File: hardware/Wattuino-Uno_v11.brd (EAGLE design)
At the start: 68.6 x 53.3 mm, 61 parts, among them IC1 ATMEGA328-PU, IC2 FT231XQ, IC3 LDO-TS1117CW-5V, IC4 LDO-TS9011-3V3, J2 USB-B-H, J3 USB-MICRO, Q1 16MHz, X1 PASSER-07, X2 PASSER-07, X3 PASSER-07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

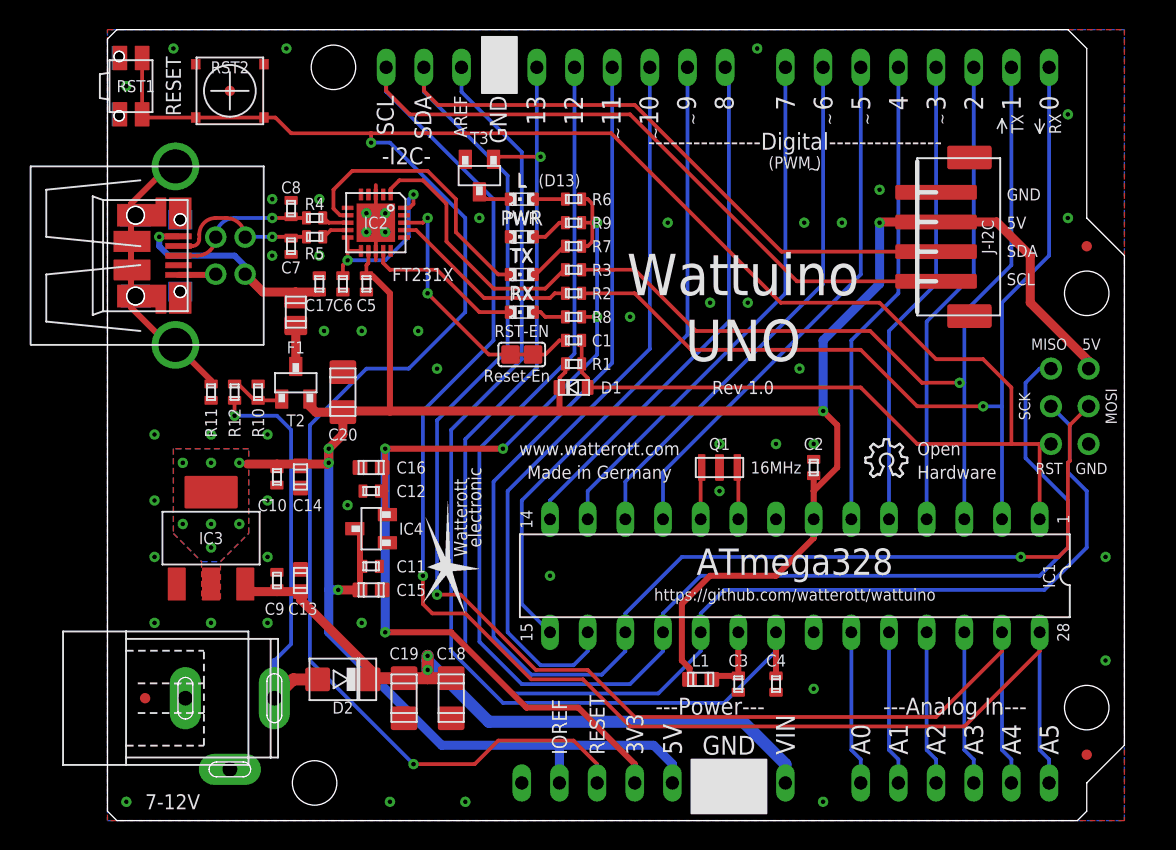
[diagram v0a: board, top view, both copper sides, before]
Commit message: updated schematics
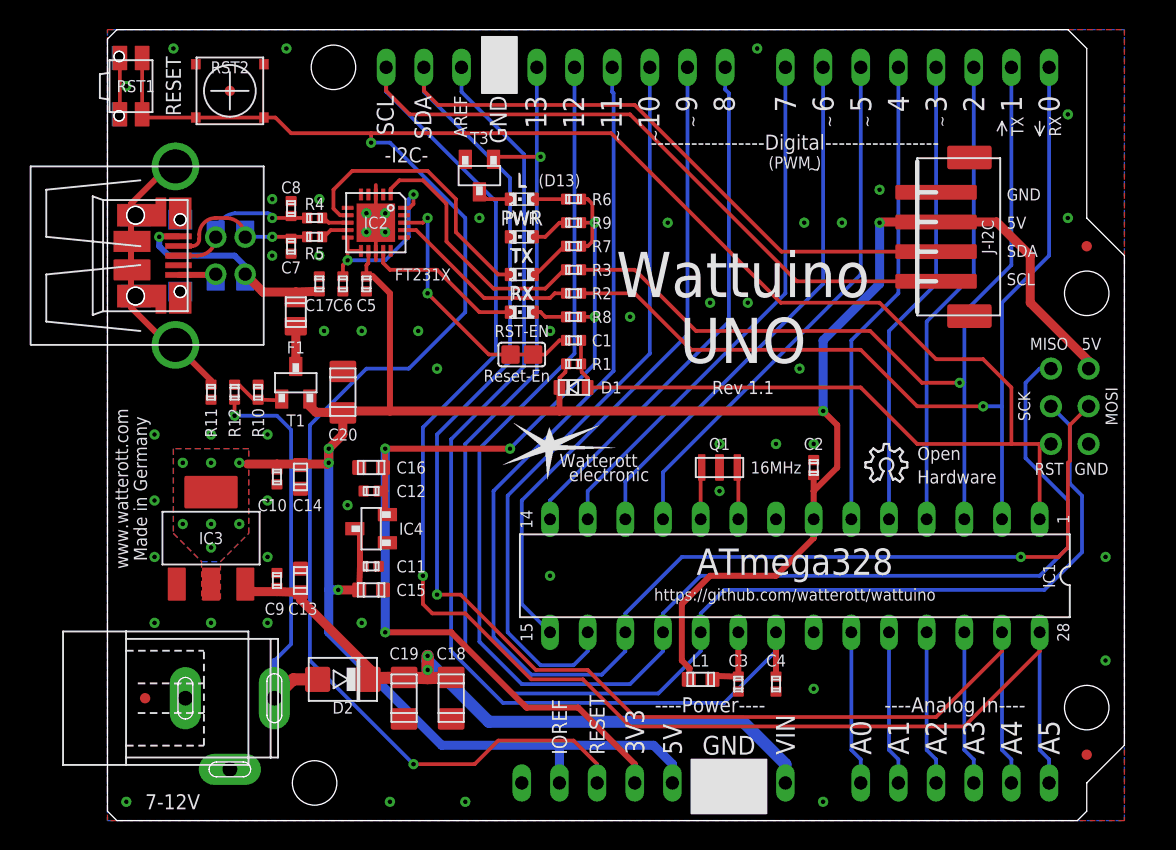
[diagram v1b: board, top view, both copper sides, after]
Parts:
- RST1: device we-switch:SW_PTS840P -> we-switch:PTS840P
- RST2: device we-switch:SW_TL3315N -> we-switch:TL3315N
- moved LOGO1 10.7 mm to (29.8, 25.2), turned to 0 degrees
- moved LOGO2 0.32 mm to (51.1, 22.9)
- renumbered T2 to T1
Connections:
- net RST: now also ARD1.RST@1, ARD1.RST@2; no longer ARD1.RST, ARD1.RST2
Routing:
- net GND: track 12.7 -> 16.9 mm, vias 51 -> 52
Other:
- board text added: "-----------------Digital-----------------"
- board text added: "----Analog In----"
- board text added: "----Power----"
- board text added: "Rev 1.1"
- board text removed: "---------------Digital---------------"
- board text removed: "---Analog In---"
- board text removed: "---Power---"
- board text removed: "Rev 1.0"

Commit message: updated schematics
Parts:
- L1: value (none) -> 10u
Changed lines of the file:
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@@
 <attribute name="VALUE" x="23.1775" y="5.3975" size="0.8128" layer="27" font="vector" ratio="10" rot="R180" align="center"/>
 </element>
-<element name="L1" library="we-rcl" package="C0603" value="" x="40.005" y="9.525" smashed="yes" rot="R90">
+<element name="L1" library="we-rcl" package="C0603" value="10u" x="40.005" y="9.525" smashed="yes" rot="R90">
 <attribute name="NAME" x="40.005" y="10.795" size="0.8128" layer="25" font="vector" ratio="10" align="center"/>
 <attribute name="VALUE" x="40.005" y="10.795" size="0.8128" layer="27" font="vector" ratio="10" align="center"/>
